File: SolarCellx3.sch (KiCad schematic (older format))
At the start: 0 parts

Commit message: finish
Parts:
- added C? (x6): 1n, symbol Device:C
- added C? (x6): 100u, symbol Main-rescue:C-Device
- added L? (x3): 10uH, symbol Main-rescue:L-Device
- added R? (x3): 330k, symbol Device:R
- added R? (x3): 768k, symbol Device:R
- added R? (x3): 1k, symbol Main-rescue:R-Device
- added SC? (x3): Solar_Cell, symbol Device:Solar_Cell
- added U? (x3): SPV1040, symbol Main-rescue:SPV1040-CustomSymbols
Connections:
- net OUT+: now also C?.1, C?.1, C?.1, R?.1, R?.1, R?.1, U?.4 (VOUT), U?.4 (VOUT), U?.4 (VOUT), U?.6 (ICTRL-), U?.6 (ICTRL-), U?.6 (ICTRL-), U?.7 (ICTRL+), U?.7 (ICTRL+), U?.7 (ICTRL+)
- net OUT-: now also C?.2, C?.2, C?.2, C?.2, C?.2, C?.2, C?.2, C?.2, C?.2, C?.2, C?.2, C?.2, R?.2, R?.2, R?.2, SC?.2 (-), SC?.2 (-), SC?.2 (-), U?.2 (GND), U?.2 (GND), U?.2 (GND)
- new net: C?.1, L?.1, R?.2, SC?.1 (+) (x3)
- new net: C?.1, R?.1, R?.2, U?.5 (VCTRL) (x3)
- new net: C?.1, R?.1, U?.1 (MPP-SET), U?.8 (XSHUT) (x3)
- new net: L?.2, U?.3 (LX) (x3)
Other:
- note added: "Inductor:\nB82442T1103K050"

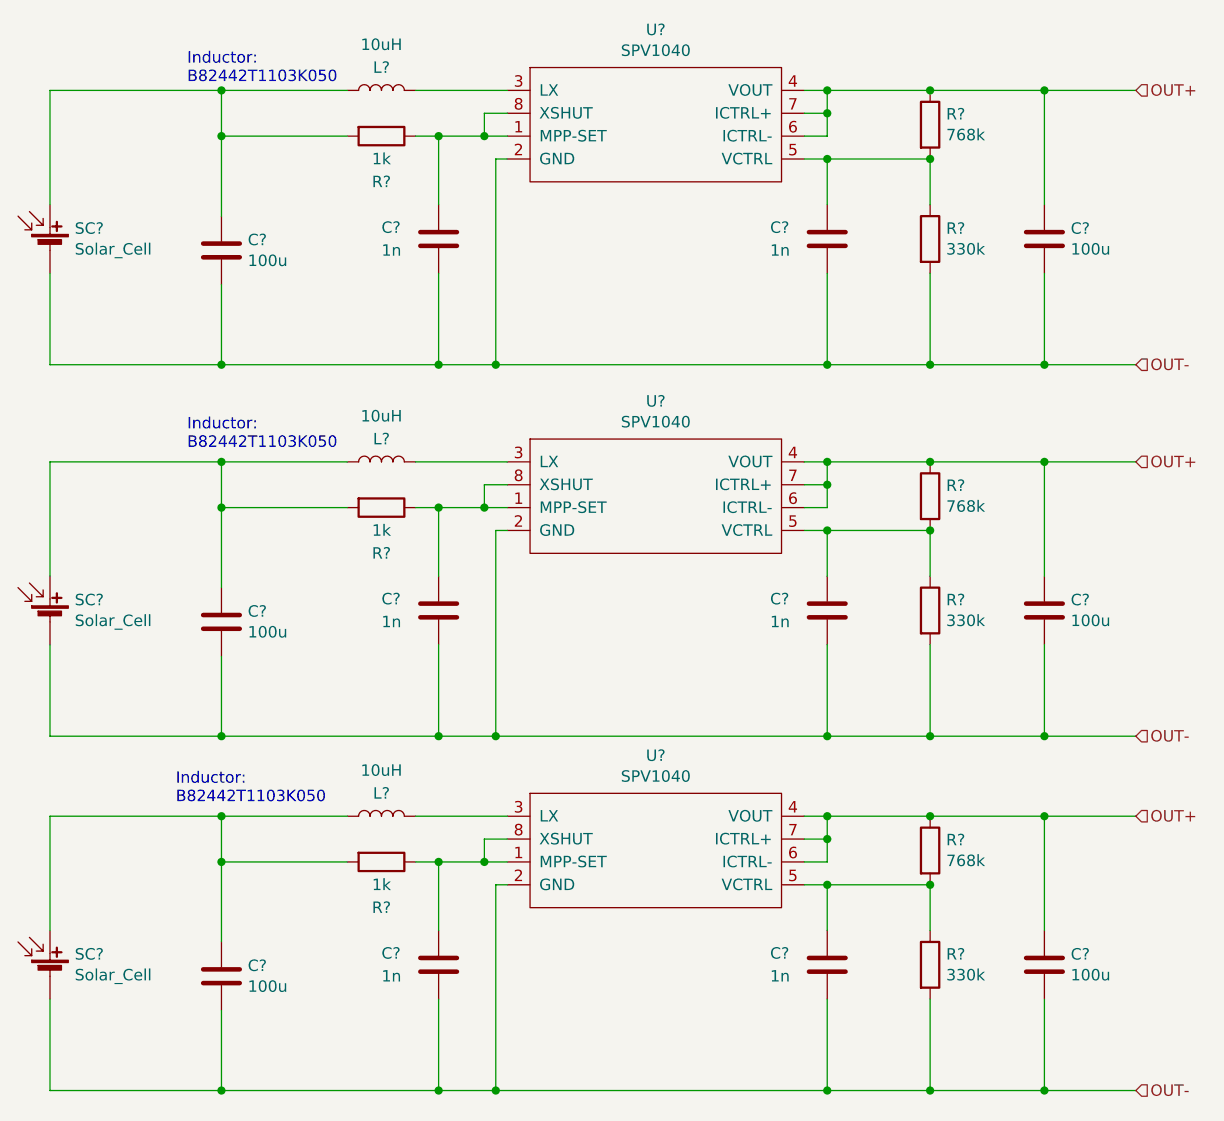
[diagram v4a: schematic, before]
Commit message: added burn wire load switches
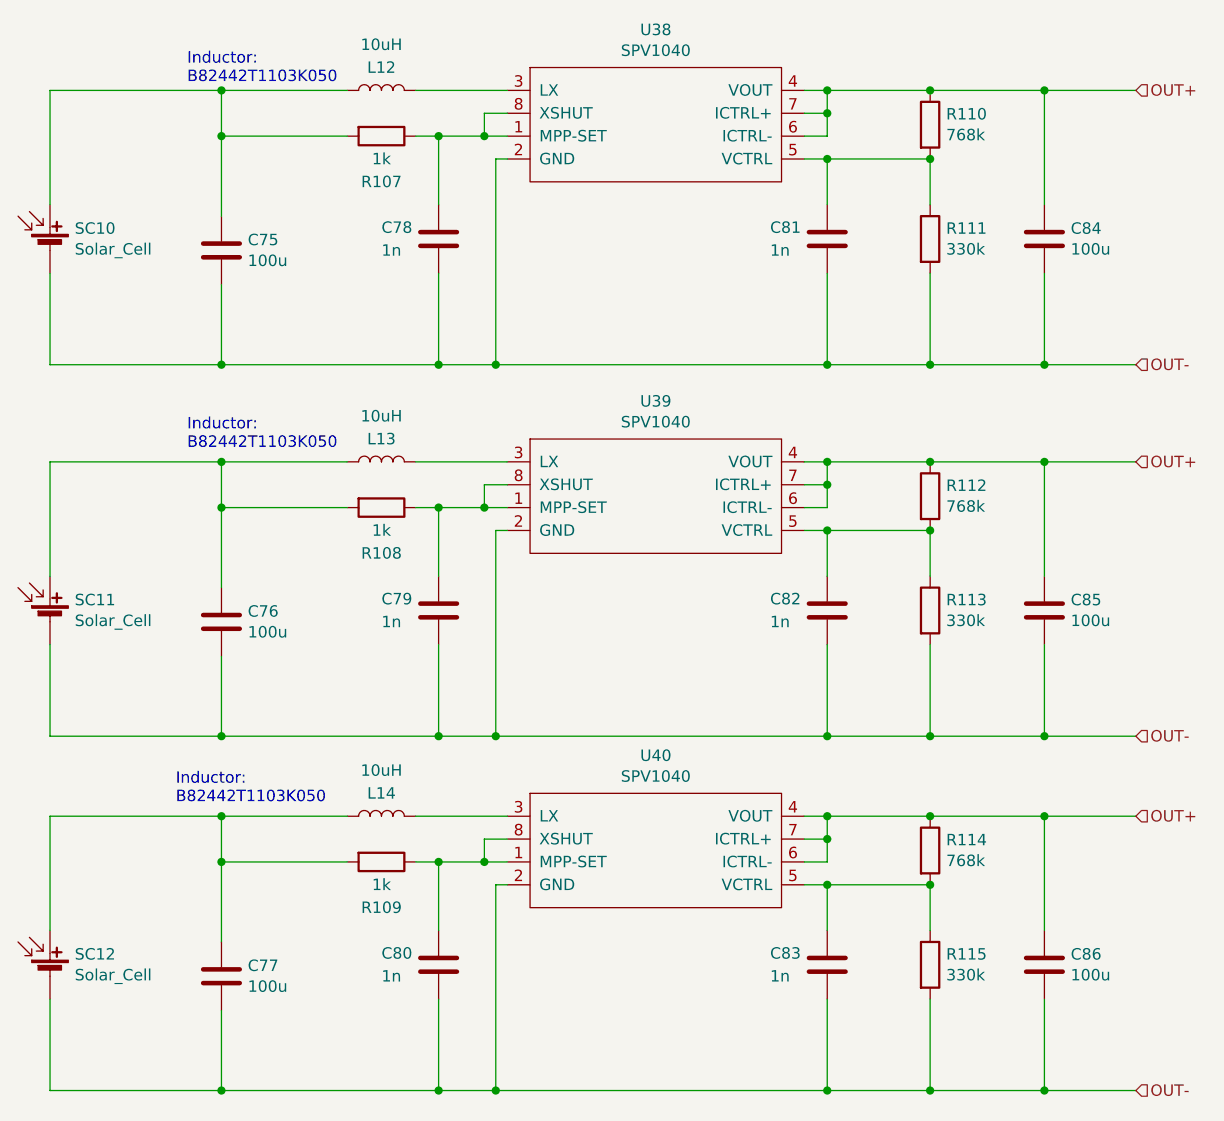
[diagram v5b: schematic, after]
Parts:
- gave numbers to parts that had none: 30
